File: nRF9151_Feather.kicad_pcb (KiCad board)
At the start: 4 copper layers, 50.8 x 22.9 mm, 148 parts, among them J1 CON-HEADER-1X12-MALE-PIN, J2 CON-HEADER-1X16-MALE-PIN, J3 CON-USB-DX07S016JA1R1500, J4 CON-S2B-PH-SM4-TB(LF)(SN), J5 CON-SM04B-SRSS-TB, J6 Conn_Coaxial, SW1 SW-434153017835‎, SW2 SW-434153017835‎, SW3 SW-434153017835‎, U1 W25Q16JVUXIQ_TR, U10 SKY65723-81, U11 TPS22919, U12 nRF9151-LAXX, U2 nPM1300-QEXX, U3 1042240820, U4 W25Q128JVPIQ, U5 RP2040, U6 SIM-ST-MFF2, U7 LIS2DH12TR, U8 TS5A3166DCKR, U9 TC7PZ14FU, Y1 Crystal_GND24

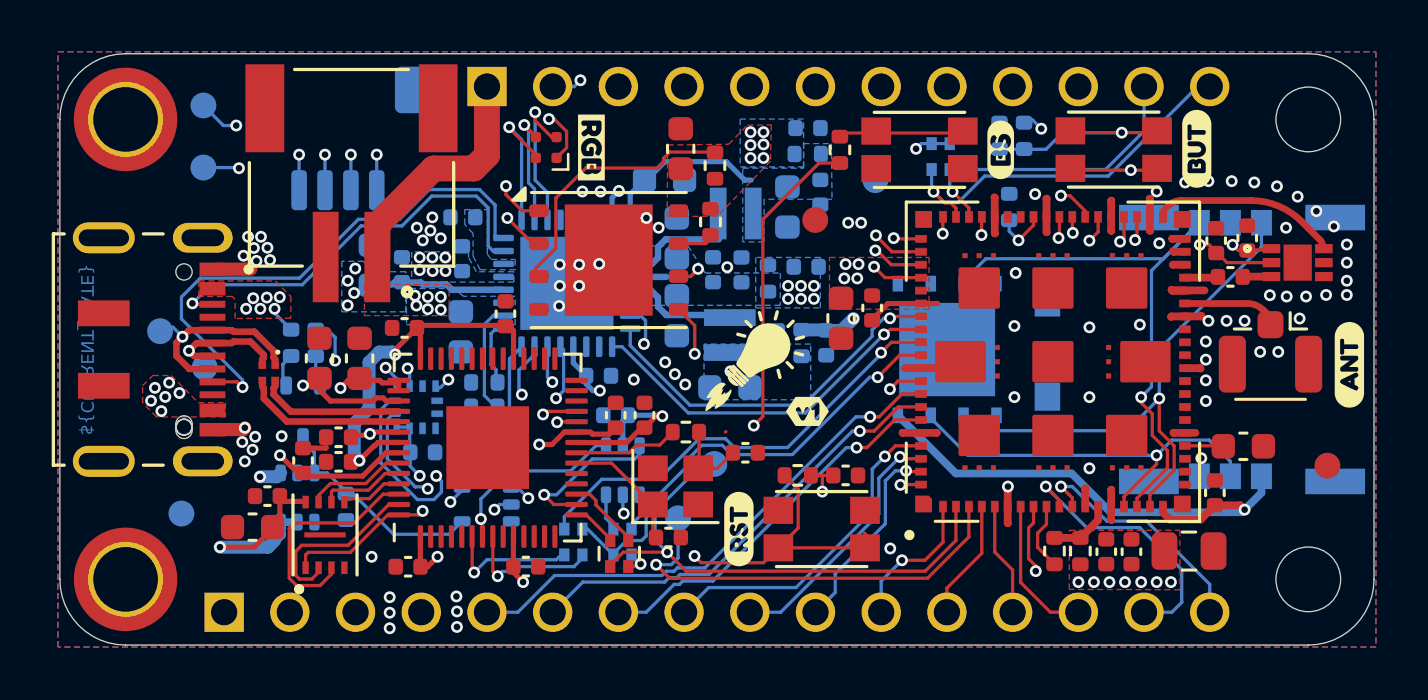
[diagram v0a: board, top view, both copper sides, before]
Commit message: Updating parts:
1. Button change
2. USB change
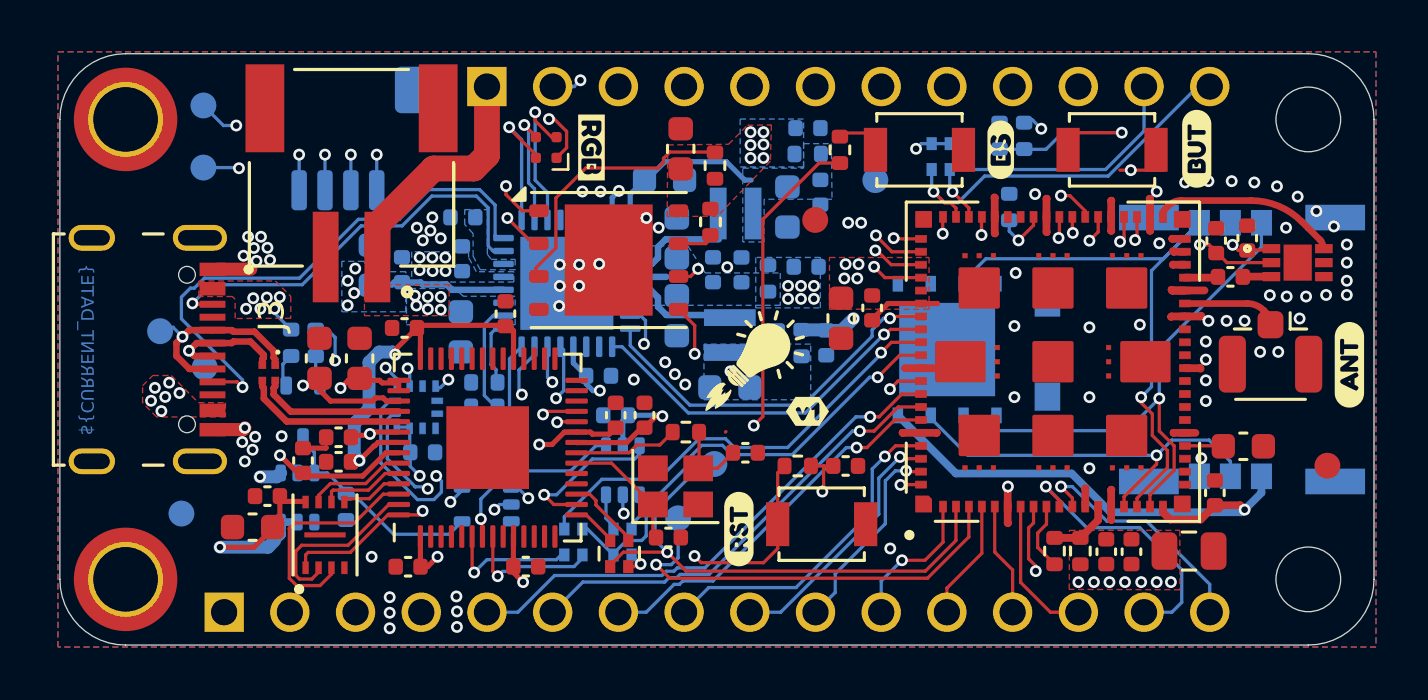
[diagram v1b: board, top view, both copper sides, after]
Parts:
- J3: value CON-USB-DX07S016JA1R1500 -> CON-USB-1003-030-01210-TR; footprint Circuit Dojo:JAE_DX07S016JA1R1500 -> Circuit Dojo:CNC_TECH_1003-030-01210-TR
- SW1, SW2, SW3: footprint Circuit Dojo:WOLFF-DEN_SW-EVP-AA402W -> Button_Switch_SMD:SW_SPST_B3U-1000P
- moved C35 0.37 mm to (153.5, 109.5)
- moved R1 0.37 mm to (151.6, 109.5)
- moved SW2 0.19 mm to (152.6, 111.8), turned to 0 degrees
- moved SW1 0.07 mm to (163.8, 97.3)
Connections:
- J2 pad 1: /Debugger/nRST -> /Headers/~{RESET}
- R1 pad 1: /Debugger/nRST -> /Headers/~{RESET}
- SW2 pad 1: /Debugger/nRST -> /Headers/~{RESET}
- U5 pad 4: unconnected-(U5-GPIO2-Pad4) -> /Debugger/nRST
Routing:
- net /Debugger/nRST: track 30.8 -> 0.00 mm, vias 1 -> 0
- net /Headers/~{RESET}: track 0.00 -> 27.1 mm, vias 0 -> 1
- net /Debugger/BOOT: track 4.90 -> 1.55 mm
- net +3V3: track 14.7 -> 13.1 mm
- net /Processor/BUTTON: track 18.8 -> 17.1 mm
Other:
- board text added: "BRD-0020-02"
- board text removed: "BRD-0020-01"

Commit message: v2 Changes:
1. Added STS4x to sensors
2. Relocated NTC away from nPM1300
3. Updated footprint for new USB connector
4. Optimized other footprint paste aperture
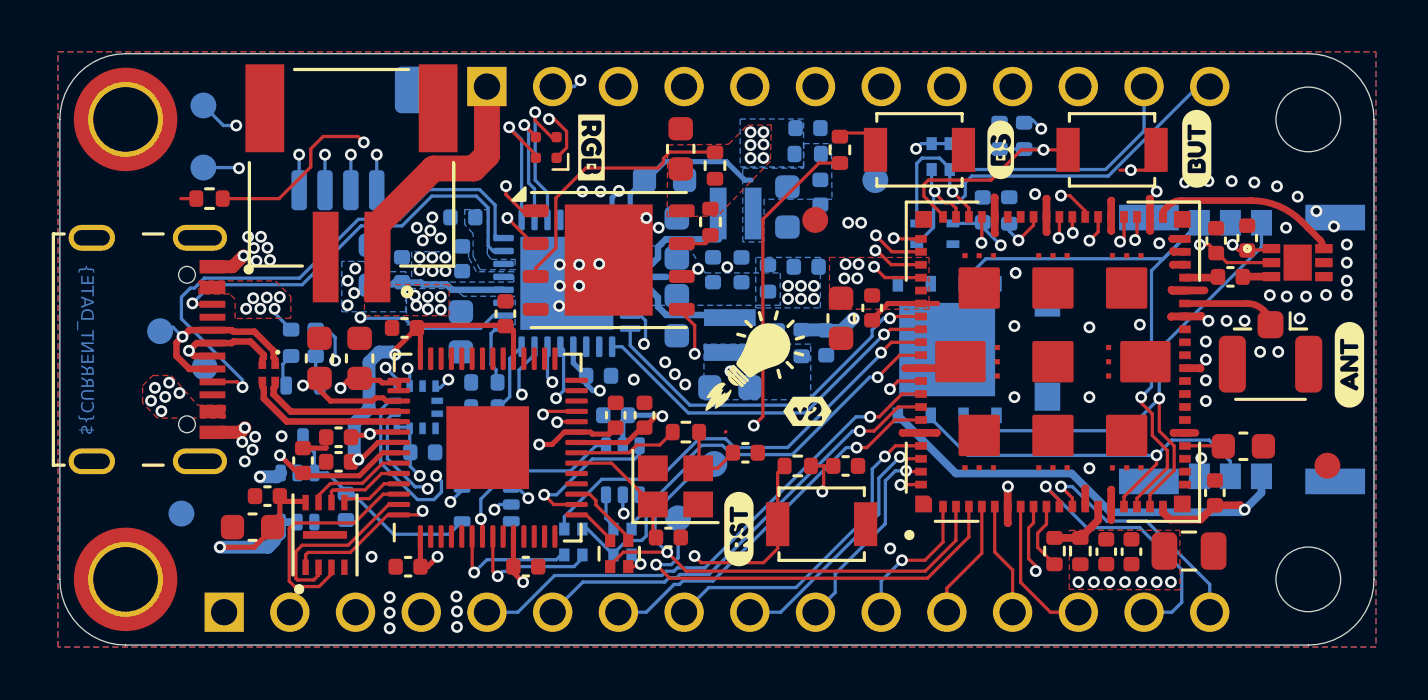
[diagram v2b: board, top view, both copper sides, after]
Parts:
- removed kibuzzard-66FC738B: G***, kibuzzard-66FC738B
- added C48: 0.1u, Capacitor_SMD:C_0402_1005Metric, B.Cu at (158.8, 99.6)
- added U13: STS4X, Circuit Dojo:STS4X, B.Cu at (156.9, 100.5)
- added kibuzzard-68937EA2: G***, kibuzzard-68937EA2, F.Cu at (152.0, 107.4)
- added kibuzzard-68A8CF71: G***, kibuzzard-68A8CF71, B.Cu at (153.9, 100.6)
- TH1: moved to F.Cu
- moved TH1 13.3 mm to (128.9, 99.2)
- moved R4 0.91 mm to (139.5, 107.2)
- moved R5 0.13 mm to (159.8, 99.6)
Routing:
- net Net-(U2-NTC): track 4.25 -> 22.5 mm, vias 0 -> 2
- net /Processor/BUTTON: track 17.1 -> 9.41 mm, vias 2 -> 1
- net /I2C_SCL: track 53.9 -> 58.1 mm
- net /I2C_SDA: track 59.9 -> 62.6 mm
- net +3V3: track 13.1 -> 15.3 mm, vias 19 -> 20
- net Net-(U2-VSET2): track 3.69 -> 2.88 mm
- net GND: track 26.6 -> 27.2 mm
- net /Headers/D8: track 15.4 -> 16.0 mm

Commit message: Fixing pinout for new USB connector
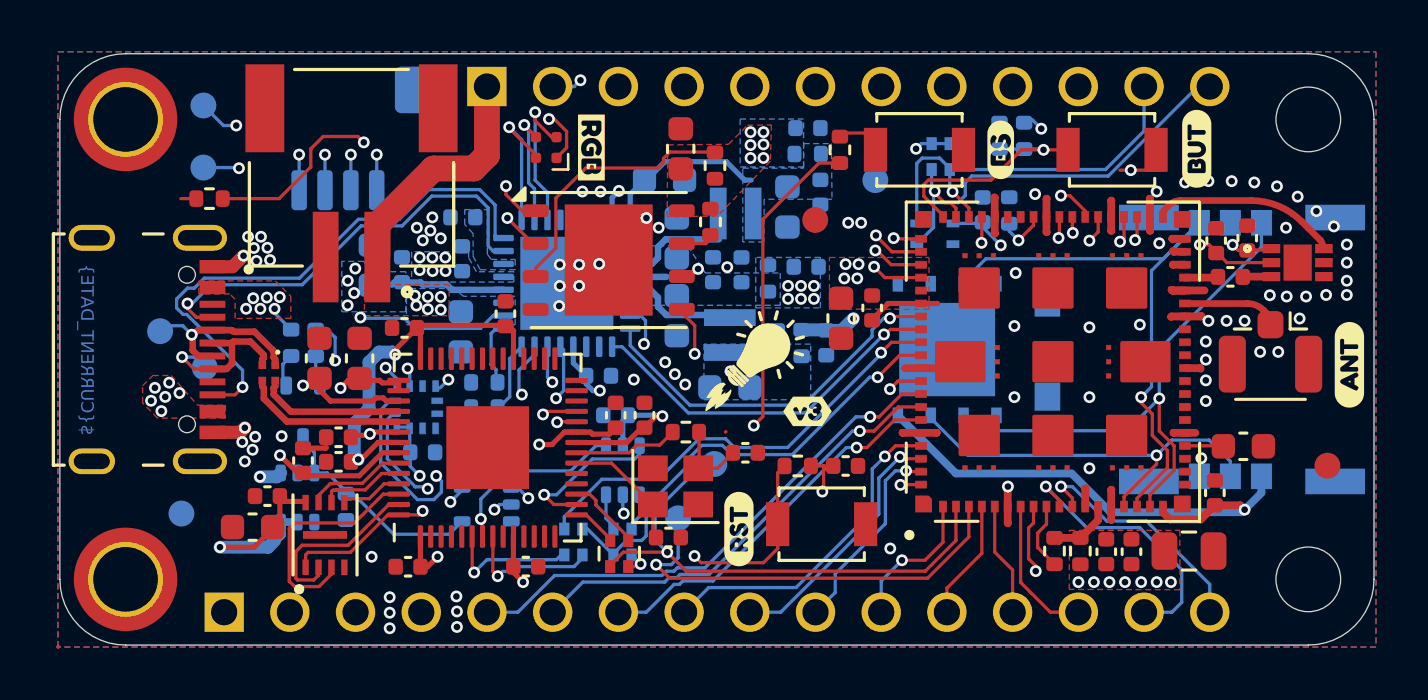
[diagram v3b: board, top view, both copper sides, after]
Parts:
- removed kibuzzard-68937EA2: G***, kibuzzard-68937EA2
- added kibuzzard-68E59538: G***, kibuzzard-68E59538, F.Cu at (152.0, 107.4)
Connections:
- J3 pad 10: unconnected-(J3-SBU1-Pad10) -> /Power/CC2
- J3 pad 3: /Power/CC1 -> unconnected-(J3-SBU2-Pad3)
- J3 pad 4: unconnected-(J3-SBU2-Pad4) -> /Power/CC1
- J3 pad 7: /Debugger/D+ -> /Debugger/D-
- J3 pad 8: /Debugger/D- -> /Debugger/D+
- J3 pad 9: /Power/CC2 -> unconnected-(J3-SBU1-Pad9)
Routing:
- net /Debugger/D-: track 8.68 -> 7.51 mm
- net /Debugger/D+: track 5.80 -> 6.84 mm
- net /Power/CC1: track 16.3 -> 16.8 mm
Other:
- board text added: "BRD-0020-03"
- board text removed: "BRD-0020-02"

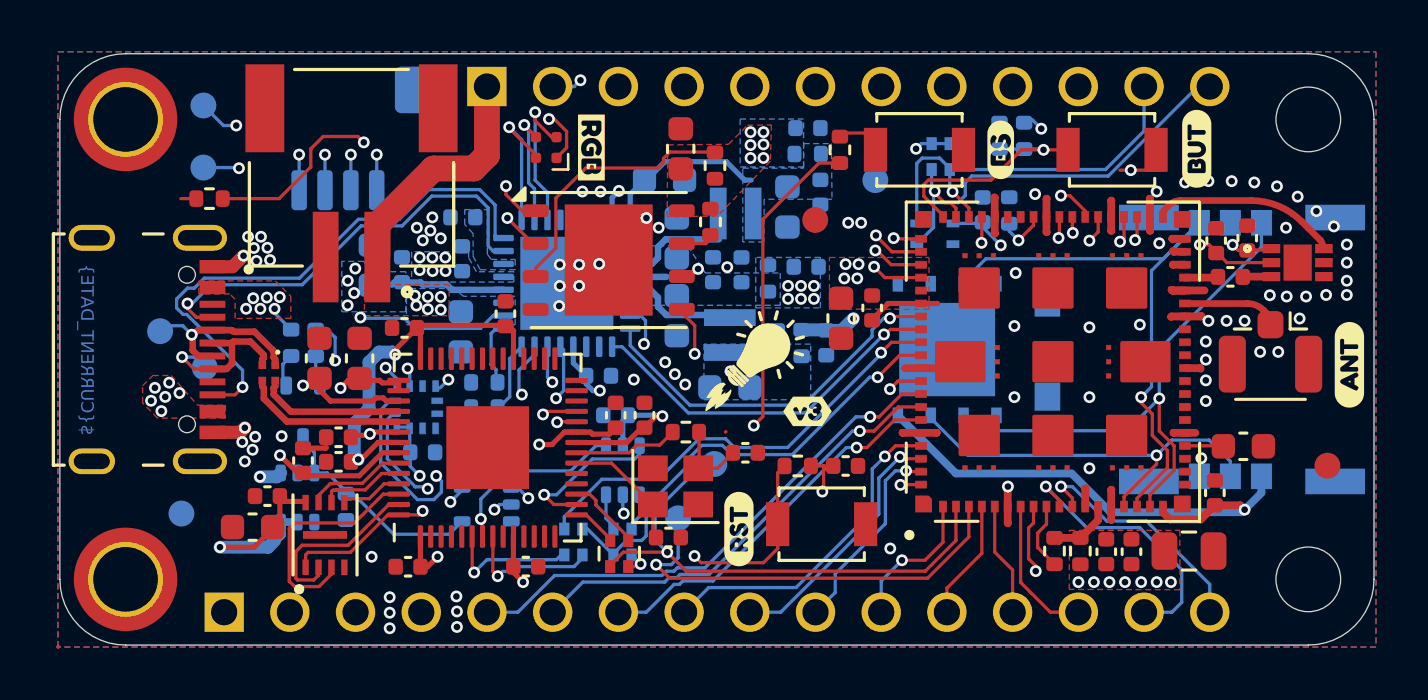
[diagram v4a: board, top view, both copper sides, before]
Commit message: PCB cleanup: reduce ground connections and set isolation to 0.2mm
- Reducing the size of ground connections
- Changing isolation to 0.2mm for all layers
- Adding border isolation 0.2mm
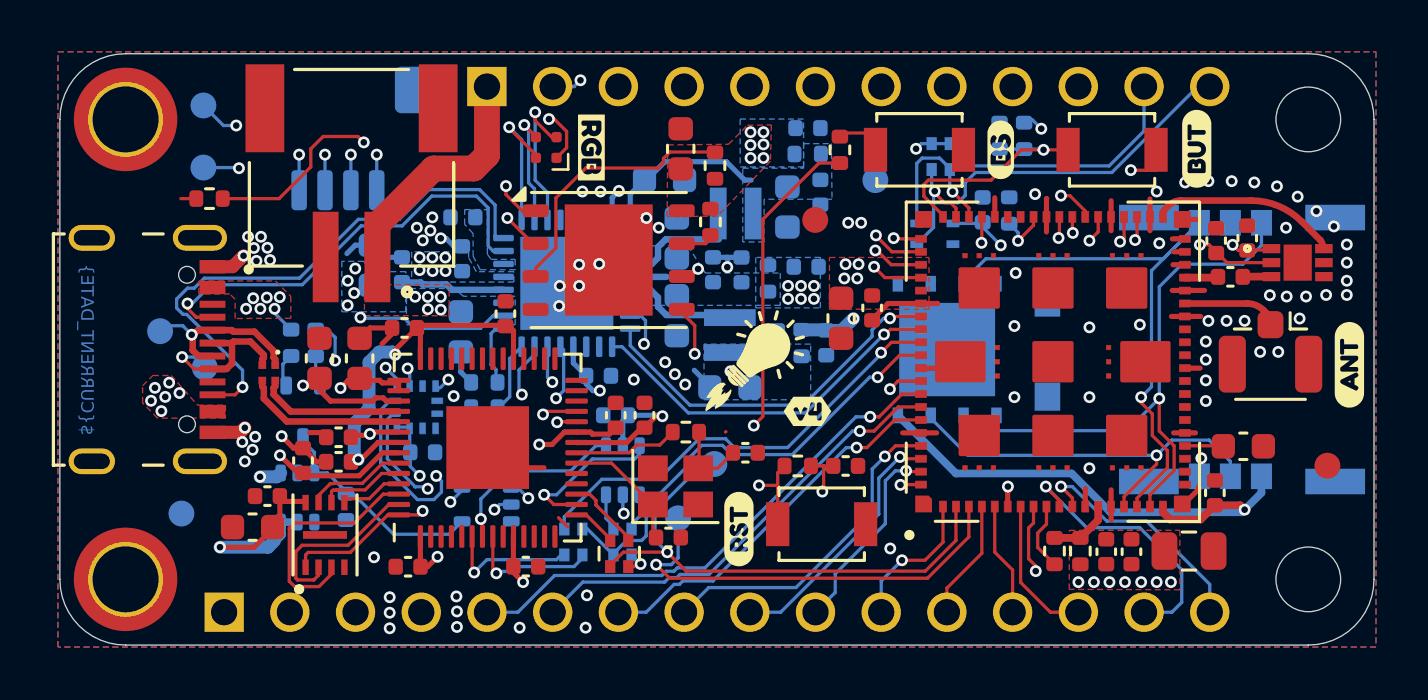
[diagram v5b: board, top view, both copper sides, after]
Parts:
- removed kibuzzard-6699D3F5: G***, kibuzzard-6699D3F5
- removed kibuzzard-68E59538: G***, kibuzzard-68E59538
- added kibuzzard-69681563: G***, kibuzzard-69681563, F.Cu at (152.0, 107.4)
- added kibuzzard-69866146: G***, kibuzzard-69866146, B.Cu at (168.7, 114.0)
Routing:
- net GND: track 27.2 -> 40.6 mm, vias 83 -> 86
- net /Processor/SIM_CLK: track 21.7 -> 23.0 mm
- net VSYS: track 57.9 -> 57.2 mm
- net /Headers/MODE/WAKE: track 41.2 -> 41.9 mm
- net /Headers/~{RESET}: track 27.1 -> 26.5 mm
- net VBAT: vias 6 -> 5
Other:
- rule pad_to_mask_clearance: 0.0508 -> 0
- board text added: "BRD-0020-04"
- board text removed: "BRD-0020-03"
